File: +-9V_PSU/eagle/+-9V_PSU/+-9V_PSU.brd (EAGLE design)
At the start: 93.7 x 71.1 mm, 27 parts, among them IC1 7809TV, IC2 7909TV

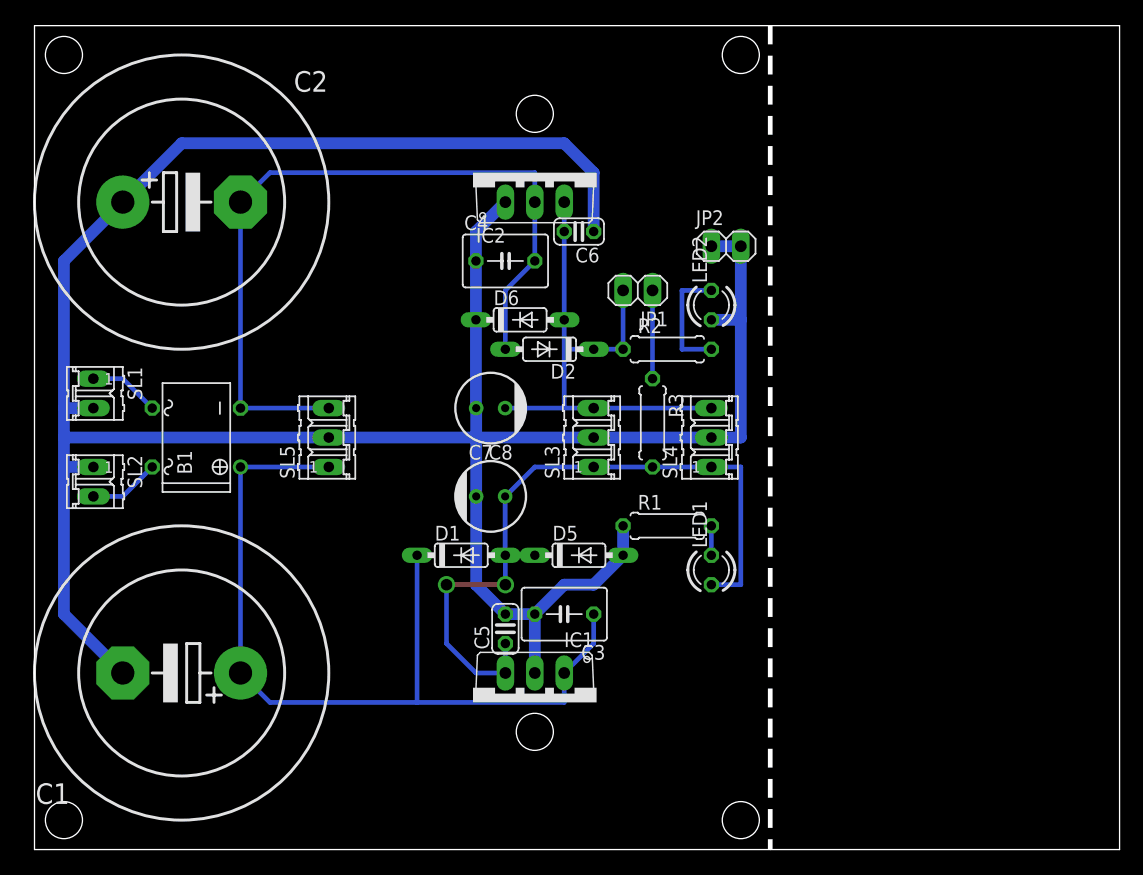
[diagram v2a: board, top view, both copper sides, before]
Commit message: Add: +/-9V PSU Case
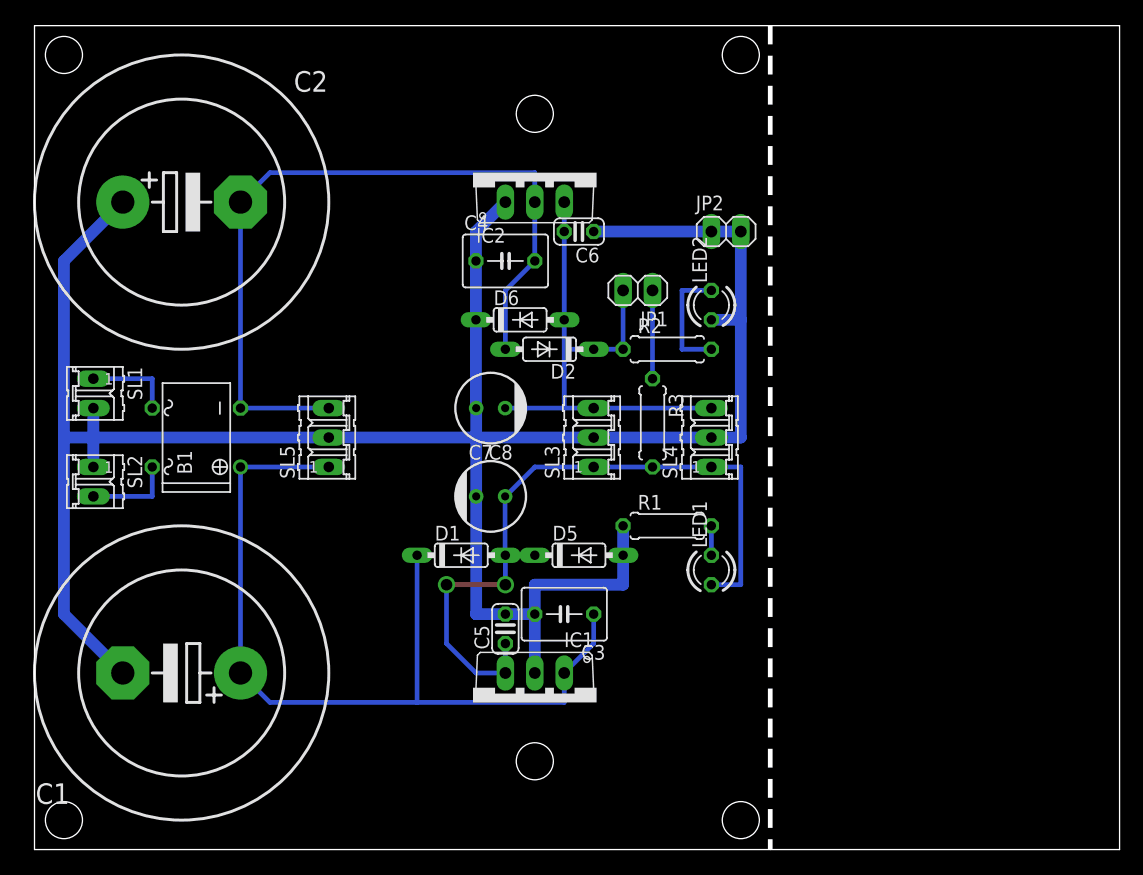
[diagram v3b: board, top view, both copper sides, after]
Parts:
- moved JP2 1.27 mm to (59.7, 53.3)
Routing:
- net GND: track 236.4 -> 203.4 mm
- net N$6: track 6.13 -> 7.62 mm
- net N$4: track 6.13 -> 7.62 mm
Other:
- board text added: "(+)"
- board text added: "(-)"
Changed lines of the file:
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@@
 <layer number="98" name="Guide" color="6" fill="1" visible="no" active="no"/>
 <layer number="99" name="SpiceOrder" color="5" fill="1" visible="no" active="no"/>
-<layer number="100" name="Grid" color="11" fill="1" visible="no" active="yes"/>
+<layer number="100" name="Grid" color="11" fill="1" visible="yes" active="yes"/>
 <layer number="200" name="200bmp" color="1" fill="10" visible="no" active="no"/>
 <layer number="201" name="tNamesOnPCB" color="5" fill="1" visible="yes" active="yes"/>
@@
 <wire x1="93.65" y1="71.11" x2="0" y2="71.11" width="0" layer="20"/>
 <wire x1="0" y1="71.11" x2="0" y2="0" width="0" layer="20"/>
-<polygon width="0" layer="41" pour="hatch">
+<polygon width="0" layer="39" pour="hatch">
 <vertex x="55.88" y="2.54"/>
 <vertex x="30.48" y="2.54"/>
@@
 <hole x="60.96" y="2.54" drill="3.2"/>
 <dimension x1="0" y1="0" x2="63.5" y2="0" x3="31.75" y3="-5.08" textsize="1.778" layer="20"/>
-<hole x="43.18" y="10.16" drill="3.2"/>
+<hole x="43.18" y="7.62" drill="3.2"/>
 <hole x="43.18" y="63.5" drill="3.2"/>
+<text x="27.94" y="5.08" size="5.08" layer="48">(+)</text>
+<text x="30.48" y="60.96" size="5.08" layer="48">(-)</text>
 </plain>
 <attributes>
@@
 <element name="R3" library="rcl" package="0207/7" value="10k" x="53.34" y="36.83" rot="R270"/>
 <element name="JP1" library="pinhead" package="1X02" value="LED" x="52.07" y="48.26" rot="R180"/>
-<element name="JP2" library="pinhead" package="1X02" value="TP_GND" x="59.69" y="52.07"/>
+<element name="JP2" library="pinhead" package="1X02" value="TP_GND" x="59.69" y="53.34"/>
 </elements>
 <signals>
@@
 <contactref element="SL5" pad="2"/>
 <wire x1="7.62" y1="55.88" x2="2.54" y2="50.8" width="1.016" layer="16"/>
-<wire x1="2.54" y1="50.8" x2="2.54" y2="38.1" width="1.016" layer="16"/>
-<wire x1="2.54" y1="38.1" x2="2.54" y2="35.56" width="1.016" layer="16"/>
-<wire x1="2.54" y1="35.56" x2="2.54" y2="33.02" width="1.016" layer="16"/>
-<wire x1="2.54" y1="33.02" x2="2.54" y2="20.32" width="1.016" layer="16"/>
+<wire x1="2.54" y1="50.8" x2="2.54" y2="35.56" width="1.016" layer="16"/>
+<wire x1="2.54" y1="35.56" x2="2.54" y2="20.32" width="1.016" layer="16"/>
 <wire x1="2.54" y1="20.32" x2="7.62" y2="15.24" width="1.016" layer="16"/>
-<wire x1="25.4" y1="35.56" x2="2.54" y2="35.56" width="1.016" layer="16"/>
-<wire x1="5.08" y1="38.1" x2="2.54" y2="38.1" width="1.016" layer="16"/>
-<wire x1="5.08" y1="33.02" x2="2.54" y2="33.02" width="1.016" layer="16"/>
+<wire x1="25.4" y1="35.56" x2="5.08" y2="35.56" width="1.016" layer="16"/>
+<wire x1="5.08" y1="35.56" x2="2.54" y2="35.56" width="1.016" layer="16"/>
 <wire x1="48.26" y1="35.56" x2="58.42" y2="35.56" width="1.016" layer="16"/>
 <wire x1="43.18" y1="15.24" x2="43.18" y2="20.32" width="1.016" layer="16"/>
@@
 <wire x1="38.1" y1="53.34" x2="38.1" y2="50.8" width="1.016" layer="16"/>
 <wire x1="38.1" y1="50.8" x2="38.1" y2="45.72" width="1.016" layer="16"/>
-<wire x1="38.1" y1="22.86" x2="40.64" y2="20.32" width="1.016" layer="16"/>
-<wire x1="40.64" y1="20.32" x2="43.18" y2="20.32" width="1.016" layer="16"/>
 <wire x1="25.4" y1="35.56" x2="38.1" y2="35.56" width="1.016" layer="16"/>
 <wire x1="38.1" y1="35.56" x2="48.26" y2="35.56" width="1.016" layer="16"/>
 <wire x1="38.1" y1="45.72" x2="38.1" y2="38.12" width="1.016" layer="16"/>
 <wire x1="38.1" y1="38.12" x2="38.12" y2="38.1" width="1.016" layer="16"/>
-<wire x1="38.12" y1="30.48" x2="38.12" y2="22.88" width="1.016" layer="16"/>
-<wire x1="38.12" y1="22.88" x2="38.1" y2="22.86" width="1.016" layer="16"/>
 <wire x1="38.12" y1="38.1" x2="38.12" y2="35.58" width="1.016" layer="16"/>
 <wire x1="38.12" y1="35.58" x2="38.1" y2="35.56" width="1.016" layer="16"/>
 <wire x1="38.12" y1="30.48" x2="38.12" y2="35.54" width="1.016" layer="16"/>
 <wire x1="38.12" y1="35.54" x2="38.1" y2="35.56" width="1.016" layer="16"/>
-<wire x1="48.26" y1="53.34" x2="48.26" y2="58.42" width="1.016" layer="16"/>
-<wire x1="48.26" y1="58.42" x2="45.72" y2="60.96" width="1.016" layer="16"/>
-<wire x1="45.72" y1="60.96" x2="12.7" y2="60.96" width="1.016" layer="16"/>
-<wire x1="12.7" y1="60.96" x2="7.62" y2="55.88" width="1.016" layer="16"/>
-<wire x1="48.26" y1="22.86" x2="50.8" y2="25.4" width="1.016" layer="16"/>
+<wire x1="50.8" y1="22.86" x2="50.8" y2="25.4" width="1.016" layer="16"/>
 <contactref element="LED2" pad="A"/>
 <wire x1="50.8" y1="27.94" x2="50.8" y2="25.4" width="1.016" layer="16"/>
@@
 <wire x1="60.96" y1="45.72" x2="60.96" y2="35.56" width="1.016" layer="16"/>
 <wire x1="60.96" y1="35.56" x2="58.42" y2="35.56" width="1.016" layer="16"/>
-<wire x1="58.42" y1="52.07" x2="60.96" y2="52.07" width="1.016" layer="16"/>
-<wire x1="60.96" y1="52.07" x2="60.96" y2="45.72" width="1.016" layer="16"/>
-<wire x1="43.18" y1="20.32" x2="45.72" y2="22.86" width="1.016" layer="16"/>
-<wire x1="45.72" y1="22.86" x2="48.26" y2="22.86" width="1.016" layer="16"/>
+<wire x1="58.42" y1="53.34" x2="60.96" y2="53.34" width="1.016" layer="16"/>
+<wire x1="60.96" y1="53.34" x2="60.96" y2="45.72" width="1.016" layer="16"/>
+<wire x1="43.18" y1="20.32" x2="43.18" y2="22.86" width="1.016" layer="16"/>
+<wire x1="43.18" y1="22.86" x2="50.8" y2="22.86" width="1.016" layer="16"/>
+<wire x1="40.64" y1="20.32" x2="38.12" y2="20.32" width="1.016" layer="16"/>
+<wire x1="38.1" y1="20.32" x2="38.12" y2="20.32" width="1.016" layer="16"/>
+<wire x1="38.12" y1="20.32" x2="38.12" y2="30.48" width="1.016" layer="16"/>
+<wire x1="40.64" y1="20.32" x2="43.18" y2="20.32" width="1.016" layer="16"/>
+<wire x1="48.26" y1="53.34" x2="58.42" y2="53.34" width="1.016" layer="16"/>
+<wire x1="5.08" y1="38.1" x2="5.08" y2="35.56" width="1.016" layer="16"/>
+<wire x1="5.08" y1="33.02" x2="5.08" y2="35.56" width="1.016" layer="16"/>
 </signal>
 <signal name="-9V">
@@
 <contactref element="B1" pad="AC1"/>
 <contactref element="SL1" pad="1"/>
-<wire x1="5.08" y1="40.64" x2="7.62" y2="40.64" width="0.4064" layer="16"/>
-<wire x1="7.62" y1="40.64" x2="10.16" y2="38.1" width="0.4064" layer="16"/>
+<wire x1="5.08" y1="40.64" x2="10.16" y2="40.64" width="0.4064" layer="16"/>
+<wire x1="10.16" y1="40.64" x2="10.16" y2="38.1" width="0.4064" layer="16"/>
 </signal>
 <signal name="N$6">
 <contactref element="B1" pad="AC2"/>
 <contactref element="SL2" pad="2"/>
-<wire x1="5.08" y1="30.48" x2="7.62" y2="30.48" width="0.4064" layer="16"/>
-<wire x1="7.62" y1="30.48" x2="10.16" y2="33.02" width="0.4064" layer="16"/>
+<wire x1="5.08" y1="30.48" x2="10.16" y2="30.48" width="0.4064" layer="16"/>
+<wire x1="10.16" y1="30.48" x2="10.16" y2="33.02" width="0.4064" layer="16"/>
 </signal>
 <signal name="+12V">
